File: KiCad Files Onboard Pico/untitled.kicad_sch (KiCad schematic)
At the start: 50 parts, among them J3 Button, J6 Conn_01x03_Male, U2 SOT-23-5 5.5V 3.3V 500mA, U4 RP2040, Y1 3225_4P 12MHz

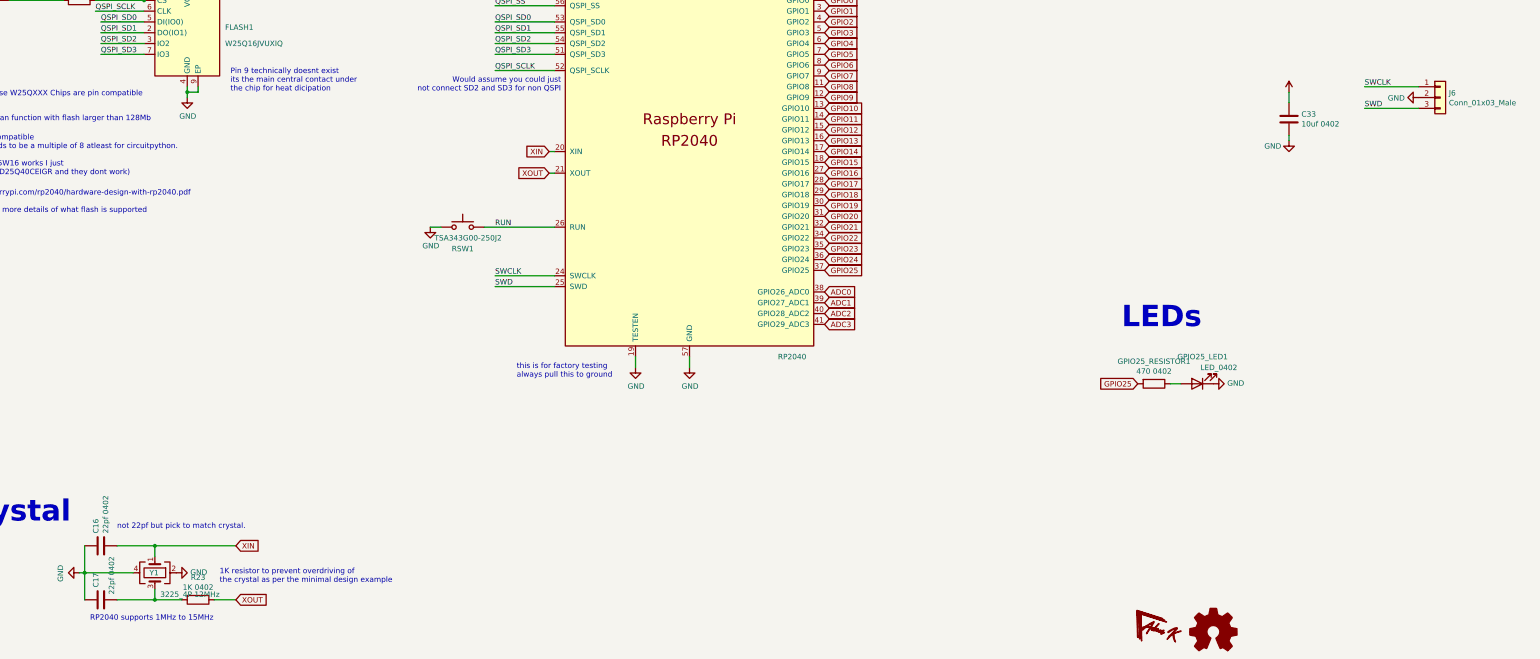
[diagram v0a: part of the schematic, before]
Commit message: Finished V1 Placement of onboard pico
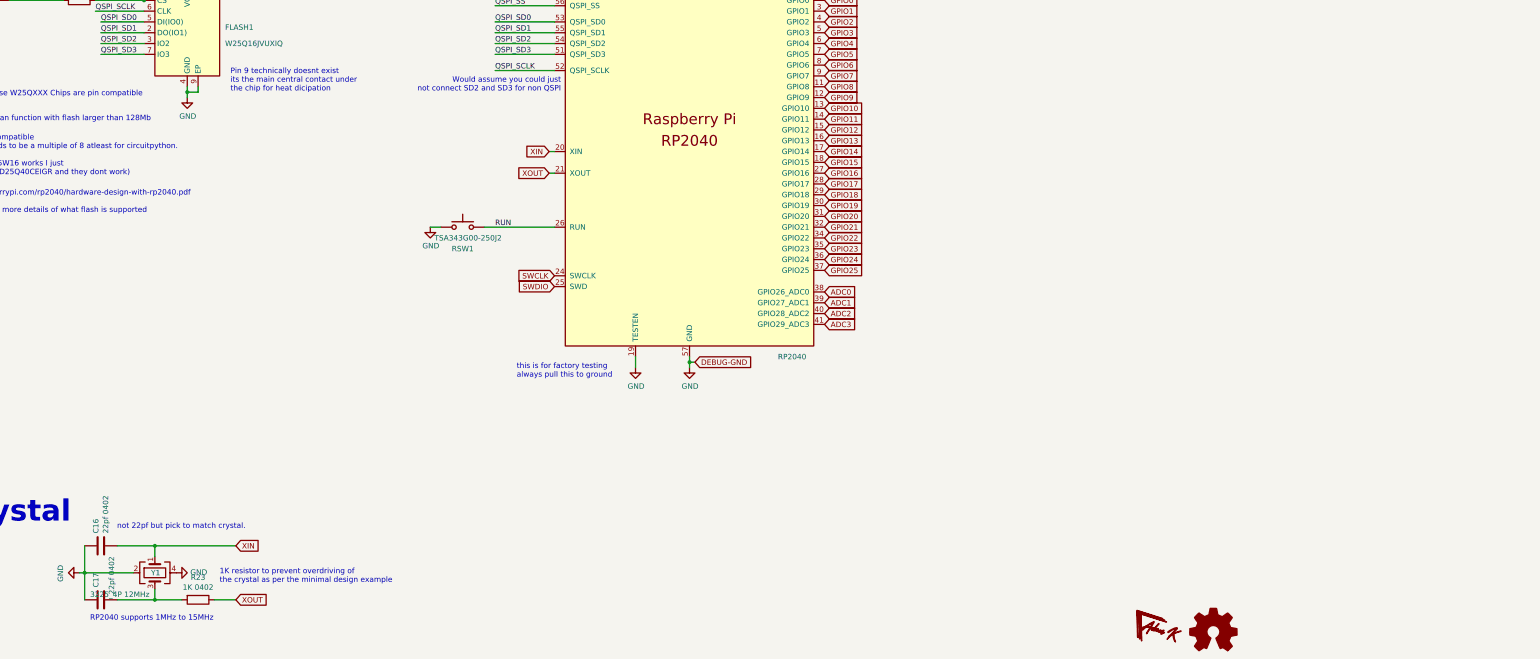
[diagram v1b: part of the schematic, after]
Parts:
- removed C33: 10uf 0402, Capacitor_SMD:C_0402_1005Metric, symbol Device:C
- removed GPIO25_LED1: LED_0402, LED_SMD:LED_0402_1005Metric, symbol Device:LED
- removed GPIO25_RESISTOR1: 470 0402, Resistor_SMD:R_0402_1005Metric, symbol Device:R
- removed J6: Conn_01x03_Male, Connector_PinHeader_2.54mm:PinHeader_1x03_P2.54mm_Vertical, symbol Connector_Generic:Conn_01x03
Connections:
- net SWD renamed SWDIO
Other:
- note removed: "LEDs"
- moved on the sheet: Y1

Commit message: fulkly wired v2
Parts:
- removed C32: 2.2uF 0402, Capacitor_SMD:C_0402_1005Metric, symbol Device:C
- removed R26: 200 0603, Resistor_SMD:R_0603_1608Metric, symbol Device:R_Small
- removed R27: 1 0402, Resistor_SMD:R_0402_1005Metric, symbol Device:R_Small
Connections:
- net +3V3: now also U4.43 (ADC_AVDD)
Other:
- note removed: "MAKE SURE THIS LINE is ran off of pin43 or close to pin43"
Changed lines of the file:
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@@
 (kicad_sch (version 20230121) (generator eeschema)
   (paper "A3")
-  (junction (at 292.1 90.17) (diameter 0) (color 0 0 0 0)
-  )
   (junction (at 139.7 44.45) (diameter 0) (color 0 0 0 0)
   )
@@
   (junction (at 212.09 81.28) (diameter 0) (color 0 0 0 0)
   )
+  (junction (at 215.9 81.28) (diameter 0) (color 0 0 0 0)
+  )
   (junction (at 273.05 60.96) (diameter 0) (color 0 0 0 0)
   )
@@
   )
   (junction (at 200.66 81.28) (diameter 0) (color 0 0 0 0)
-  )
-  (junction (at 292.1 78.74) (diameter 0) (color 0 0 0 0)
   )
   (junction (at 181.61 81.28) (diameter 0) (color 0 0 0 0)
@@
     (stroke (width 0) (type default))
   )
-  (wire (pts (xy 215.9 90.17) (xy 292.1 90.17))
-    (stroke (width 0) (type default))
-  )
   (wire (pts (xy 237.49 96.52) (xy 242.57 96.52))
     (stroke (width 0) (type default))
@@
     (stroke (width 0) (type default))
   )
-  (wire (pts (xy 292.1 78.74) (xy 292.1 81.28))
-    (stroke (width 0) (type default))
-  )
-  (wire (pts (xy 292.1 90.17) (xy 292.1 86.36))
-    (stroke (width 0) (type default))
-  )
   (wire (pts (xy 119.38 44.45) (xy 139.7 44.45))
     (stroke (width 0) (type default))
@@
     (stroke (width 0) (type default))
   )
-  (wire (pts (xy 215.9 93.98) (xy 215.9 90.17))
+  (wire (pts (xy 215.9 73.66) (xy 215.9 81.28))
     (stroke (width 0) (type default))
   )
@@
     (stroke (width 0) (type default))
   )
-  (wire (pts (xy 292.1 67.31) (xy 292.1 69.85))
-    (stroke (width 0) (type default))
-  )
   (wire (pts (xy 179.07 60.96) (xy 179.07 81.28))
     (stroke (width 0) (type default))
@@
     (stroke (width 0) (type default))
   )
+  (wire (pts (xy 215.9 81.28) (xy 215.9 93.98))
+    (stroke (width 0) (type default))
+  )
   (wire (pts (xy 15.24 87.63) (xy 26.67 87.63))
     (stroke (width 0) (type default))
@@
     (stroke (width 0) (type default))
   )
-  (wire (pts (xy 215.9 73.66) (xy 215.9 81.28))
-    (stroke (width 0) (type default))
-  )
   (wire (pts (xy 81.28 87.63) (xy 81.28 91.44))
     (stroke (width 0) (type default))
@@
     (stroke (width 0) (type default))
   )
-  (wire (pts (xy 292.1 74.93) (xy 292.1 78.74))
-    (stroke (width 0) (type default))
-  )
   (wire (pts (xy 87.63 96.52) (xy 87.63 97.79))
     (stroke (width 0) (type default))
@@
     (stroke (width 0) (type default))
   )
-  (wire (pts (xy 292.1 102.87) (xy 292.1 105.41))
-    (stroke (width 0) (type default))
-  )
   (wire (pts (xy 179.07 81.28) (xy 172.72 81.28))
     (stroke (width 0) (type default))
@@
   )
   (wire (pts (xy 215.9 60.96) (xy 215.9 73.66))
-    (stroke (width 0) (type default))
-  )
-  (wire (pts (xy 292.1 90.17) (xy 292.1 95.25))
-    (stroke (width 0) (type default))
-  )
-  (wire (pts (xy 292.1 78.74) (xy 306.07 78.74))
     (stroke (width 0) (type default))
   )
@@
   (text "RP2040 supports 1MHz to 15MHz" (at 58.42 257.81 0)
     (effects (font (size 1.27 1.27)) (justify left bottom))
-  )
-  (text "MAKE SURE THIS LINE \nis ran off of pin43\nor close to pin43"
-    (at 289.56 78.74 90)
-    (effects (font (size 0.5 0.5)) (justify left bottom))
   )
   (text "https://datasheets.raspberrypi.com/rp2040/hardware-design-with-rp2040.pdf\n\nOn page 13 you can learn more details of what flash is supported\n"
@@
   (label "QSPI_SD0" (at 153.67 116.84 0) (fields_autoplaced)
     (effects (font (size 1.27 1.27)) (justify left bottom))
-  )
-  (label "ADC_VREF" (at 306.07 78.74 180) (fields_autoplaced)
-    (effects (font (size 1.27 1.27)) (justify right bottom))
   )
   (label "QSPI_SD3" (at 153.67 124.46 0) (fields_autoplaced)
@@
         (path "/7b892ee5-f34f-4bca-8f87-a56522432f7c"
           (reference "#PWR06") (unit 1)
-        )
-      )
-    )
-  )
-  (symbol (lib_id "power:GND") (at 292.1 105.41 0) (unit 1)
-    (in_bom yes) (on_board yes) (dnp no)
-    (property "Reference" "#PWR079" (at 292.1 111.76 0)
-      (effects (font (size 1.27 1.27)) hide)
-    )
-    (property "Value" "GND" (at 292.227 109.8042 0)
-      (effects (font (size 1.27 1.27)))
-    )
-    (property "Footprint" "" (at 292.1 105.41 0)
-      (effects (font (size 1.27 1.27)) hide)
-    )
-    (property "Datasheet" "" (at 292.1 105.41 0)
-      (effects (font (size 1.27 1.27)) hide)
-    )
-    (pin "1")
-    (instances
-      (project "Env-MicroDotClock"
-        (path "/3dbeb8d8-208e-4f6d-8d30-b14372f68a4f/6b5c3b7c-d164-4e63-b354-b3df0a72db3d"
-          (reference "#PWR079") (unit 1)
-        )
-      )
-      (project "EnvOpenPico"
-        (path "/7b892ee5-f34f-4bca-8f87-a56522432f7c"
-          (reference "#PWR0101") (unit 1)
         )
       )
@@
     )
   )
-  (symbol (lib_id "Device:C") (at 292.1 99.06 0) (unit 1)
-    (in_bom yes) (on_board yes) (dnp no)
-    (property "Reference" "C32" (at 292.1 99.06 0)
-      (effects (font (size 0.5 0.5)))
-    )
-    (property "Value" "2.2uF 0402" (at 288.29 104.14 90)
-      (effects (font (size 1.27 1.27)) (justify left))
-    )
-    (property "Footprint" "Capacitor_SMD:C_0402_1005Metric" (at 293.0652 102.87 0)
-      (effects (font (size 1.27 1.27)) hide)
-    )
-    (property "Datasheet" "" (at 292.1 99.06 0)
-      (effects (font (size 1.27 1.27)) hide)
-    )
-    (property "LCSC" " " (at 292.1 99.06 0)
-      (effects (font (size 1.27 1.27)) hide)
-    )
-    (pin "1")
-    (pin "2")
-    (instances
-      (project "Env-MicroDotClock"
-        (path "/3dbeb8d8-208e-4f6d-8d30-b14372f68a4f/6b5c3b7c-d164-4e63-b354-b3df0a72db3d"
-          (reference "C32") (unit 1)
-        )
-      )
-      (project "EnvOpenPico"
-        (path "/7b892ee5-f34f-4bca-8f87-a56522432f7c"
-          (reference "C102") (unit 1)
-        )
-      )
-    )
-  )
   (symbol (lib_id "Regulator_Linear:AP131-15") (at 111.76 46.99 0) (unit 1)
     (in_bom yes) (on_board yes) (dnp no)
@@
     )
   )
-  (symbol (lib_id "power:+3.3V") (at 292.1 67.31 0) (unit 1)
-    (in_bom yes) (on_board yes) (dnp no)
-    (property "Reference" "#PWR078" (at 292.1 71.12 0)
-      (effects (font (size 1.27 1.27)) hide)
-    )
-    (property "Value" "+3.3V" (at 292.481 62.9158 0)
-      (effects (font (size 1.27 1.27)))
-    )
-    (property "Footprint" "" (at 292.1 67.31 0)
-      (effects (font (size 1.27 1.27)) hide)
-    )
-    (property "Datasheet" "" (at 292.1 67.31 0)
-      (effects (font (size 1.27 1.27)) hide)
-    )
-    (pin "1")
-    (instances
-      (project "Env-MicroDotClock"
-        (path "/3dbeb8d8-208e-4f6d-8d30-b14372f68a4f/6b5c3b7c-d164-4e63-b354-b3df0a72db3d"
-          (reference "#PWR078") (unit 1)
-        )
-      )
-      (project "EnvOpenPico"
-        (path "/7b892ee5-f34f-4bca-8f87-a56522432f7c"
-          (reference "#PWR013") (unit 1)
-        )
-      )
-    )
-  )
   (symbol (lib_id "power:GND") (at 81.28 134.62 0) (unit 1)
     (in_bom yes) (on_board yes) (dnp no)
@@
     )
   )
-  (symbol (lib_id "Device:R_Small") (at 292.1 83.82 0) (unit 1)
-    (in_bom yes) (on_board yes) (dnp no)
-    (property "Reference" "R27" (at 293.5986 82.6516 0)
-      (effects (font (size 1.27 1.27)) (justify left))
-    )
-    (property "Value" "1 0402" (at 293.5986 84.963 0)
-      (effects (font (size 1.27 1.27)) (justify left))
-    )
-    (property "Footprint" "Resistor_SMD:R_0402_1005Metric" (at 292.1 83.82 0)
-      (effects (font (size 1.27 1.27)) hide)
-    )
-    (property "Datasheet" "" (at 292.1 83.82 0)
-      (effects (font (size 1.27 1.27)) hide)
-    )
-    (property "LCSC" " " (at 292.1 83.82 0)
-      (effects (font (size 1.27 1.27)) hide)
-    )
-    (pin "1")
-    (pin "2")
-    (instances
-      (project "Env-MicroDotClock"
-        (path "/3dbeb8d8-208e-4f6d-8d30-b14372f68a4f/6b5c3b7c-d164-4e63-b354-b3df0a72db3d"
-          (reference "R27") (unit 1)
-        )
-      )
-      (project "EnvOpenPico"
-        (path "/7b892ee5-f34f-4bca-8f87-a56522432f7c"
-          (reference "R10") (unit 1)
-        )
-      )
-    )
-  )
   (symbol (lib_id "Device:FerriteBead_Small") (at 91.44 44.45 90) (unit 1)
     (in_bom yes) (on_board yes) (dnp no) (fields_autoplaced)
@@
         )
       )
-    )
-  )
-  (symbol (lib_id "Device:R_Small") (at 292.1 72.39 0) (unit 1)
-    (in_bom yes) (on_board yes) (dnp no)
-    (property "Reference" "R26" (at 293.5986 71.2216 0)
-      (effects (font (size 1.27 1.27)) (justify left))
-    )
-    (property "Value" "200 0603" (at 293.5986 73.533 0)
-      (effects (font (size 1.27 1.27)) (justify left))
-    )
-    (property "Footprint" "Resistor_SMD:R_0603_1608Metric" (at 292.1 72.39 0)
-      (effects (font (size 1.27 1.27)) hide)
-    )
-    (property "Datasheet" "" (at 292.1 72.39 0)
-      (effects (font (size 1.27 1.27)) hide)
-    )
-    (property "LCSC" " " (at 292.1 72.39 0)
-      (effects (font (size 1.27 1.27)) hide)
-    )
-    (pin "1")
-    (pin "2")
-    (instances
-      (project "Env-MicroDotClock"
-        (path "/3dbeb8d8-208e-4f6d-8d30-b14372f68a4f/6b5c3b7c-d164-4e63-b354-b3df0a72db3d"
-          (reference "R26") (unit 1)
-        )
-      )
-      (project "EnvOpenPico"
-        (path "/7b892ee5-f34f-4bca-8f87-a56522432f7c"
-          (reference "R9") (unit 1)
-        )
-      )

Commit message: began rework of onboard 2040 pcb
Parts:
- removed C15: 0.1uf 0402, Capacitor_SMD:C_0402_1005Metric, symbol Device:C
- removed NT1: NetTie_2, NetTie:NetTie-2_SMD_Pad0.5mm, symbol Device:NetTie_2
- removed R17: 220 0402, Resistor_SMD:R_0402_1005Metric, symbol Device:R
- removed R19: 5.6K 0402, Resistor_SMD:R_0402_1005Metric, symbol Device:R
- removed R20: 10K 0402, Resistor_SMD:R_0402_1005Metric, symbol Device:R
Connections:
- net GND: now also USB1.13 (SHIELD)
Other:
- note removed: "I think this is important for usb 3.0 but not 2.0 and 1.1 however it may help with analogue performance but ive yet to test this"
- note removed: "VBUS SENSE"

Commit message: finished up and cleaned up PCB, added logos
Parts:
- U2: value SOT-23-5 5.5V 3.3V 500mA -> TLV75733PDBVR
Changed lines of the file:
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@@
       (effects (font (size 1.27 1.27)))
     )
-    (property "Value" "SOT-23-5 5.5V 3.3V 500mA" (at 111.76 40.6146 0)
+    (property "Value" "TLV75733PDBVR" (at 111.76 40.6146 0)
       (effects (font (size 1.27 1.27)))
     )

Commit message: added thermal vias, improved gnd connections from IS31FL37s, added thermal vias, added power only usb port on the back.
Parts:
- removed USB1: TYPE-C-31-M-12, Connector_USB:USB_C_Receptacle_HRO_TYPE-C-31-M-12, symbol Type-C:HRO-TYPE-C-31-M-12
- added D2: 1N4002W, Diode_SMD:D_SOD-123, symbol Device:D_Schottky
- added J2: GT-USB-7051A, Connector_USB:USB_C_Receptacle_G-Switch_GT-USB-7051x, symbol Connector:USB_C_Receptacle_USB2.0_16P
- added J4: TYPE-C-31-M-12, Connector_USB:USB_C_Receptacle_HRO_TYPE-C-31-M-12, symbol Connector:USB_C_Receptacle_USB2.0_16P
- added R14, R17: 5.1K 0805, Resistor_SMD:R_0805_2012Metric, symbol Device:R_Small
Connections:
- net GND: now also J2.A1 (GND), J2.A12 (GND), J2.B1 (GND), J2.B12 (GND), J2.S1 (SHIELD), J4.A1 (GND), J4.A12 (GND), J4.B1 (GND), J4.B12 (GND), J4.S1 (SHIELD), R14.1, R17.1
- net USB_D+: now also J4.A6 (D+), J4.B6 (D+)
- net USB_D-: now also J4.A7 (D-), J4.B7 (D-)
- net VBUS: now also J4.A4 (VBUS), J4.A9 (VBUS), J4.B4 (VBUS), J4.B9 (VBUS)
- net VSYS: now also D2.1 (K)
- net at R16.2: now also J4.A5 (CC1)
- net at R15.2: now also J4.B5 (CC2)
- new net: J2.A5 (CC1), R14.2
- new net: D2.2 (A), J2.A4 (VBUS), J2.A9 (VBUS), J2.B4 (VBUS), J2.B9 (VBUS)
- new net: J2.B5 (CC2), R17.2
- no-connect marks 2 -> 0
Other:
- moved on the sheet: D1, R15, R16

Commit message: swapped LDO for more capable switching regulator.
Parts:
- removed C19, C20, CBP1: 10uf 0402, Capacitor_SMD:C_0402_1005Metric, symbol Device:C
- removed F1: 0805L050WR, Fuse:Fuse_0805_2012Metric, symbol Device:Polyfuse_Small
- removed FB1: FerriteBead 0402, Resistor_SMD:R_0402_1005Metric, symbol Device:FerriteBead_Small
- removed R22: 100K 0402, Resistor_SMD:R_0402_1005Metric, symbol Device:R
- removed U2: TLV75733PDBVR, Package_TO_SOT_SMD:SOT-23-5, symbol Regulator_Linear:AP131-15
- added C15, C20, C32: 10uF 0402, Capacitor_SMD:C_0402_1005Metric, symbol Device:C_Small
- added C19: 0.1uF 0402, Capacitor_SMD:C_0402_1005Metric, symbol Device:C_Small
- added L1: SPH3015H2R2MT, Inductor_SMD:L_Sunlord_SWPA3015S, symbol Device:L_Small
- added R19: 100ohm 0402, Resistor_SMD:R_0402_1005Metric, symbol Device:R_Small
- added U2: TPS63001DRCR, Package_SON:Texas_DRC0010J_ThermalVias, symbol Regulator_Switching:TPS63001
- D1, D2: value 1N4002W -> 1N5819W
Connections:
- net +3V3: now also C20.1, C32.1, U2.1 (VOUT), U2.10 (FB)
- net GND: now also C15.2, C19.2, C20.2, C32.2, U2.11 (PGND), U2.3 (PGND), U2.9 (GND)
- net VSYS: now also C15.1, R19.1, U2.5 (VIN)
- net VBUS: no longer names the net of D1.2 (A), J4.A4 (VBUS), J4.A9 (VBUS), J4.B4 (VBUS), J4.B9 (VBUS)
- new net: L1.1, U2.4 (L1)
- new net: L1.2, U2.2 (L2)
- new net: C19.1, R19.2, U2.6 (EN), U2.7 (PS/SYNC), U2.8 (VINA)
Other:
- note removed: "500mA hold current 1A trip 6V trip"
- note removed: "D1 NEEDS to be 0omh resistor or 1N4002 diode"
- note removed: "GPIOs"
- note removed: "Only fit cBP1 if you have selected an alternate voltage regulator TLV75533PDBVR does not require cBP1."
- note removed: "USB/POWER"

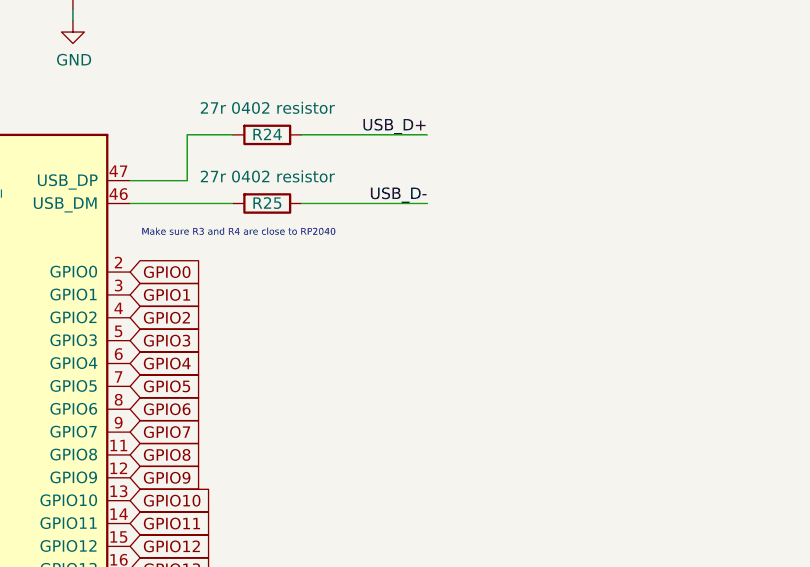
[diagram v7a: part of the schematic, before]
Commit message: Moved all ICs to one i2c bus, removed SI7021, added i2c level shifters.
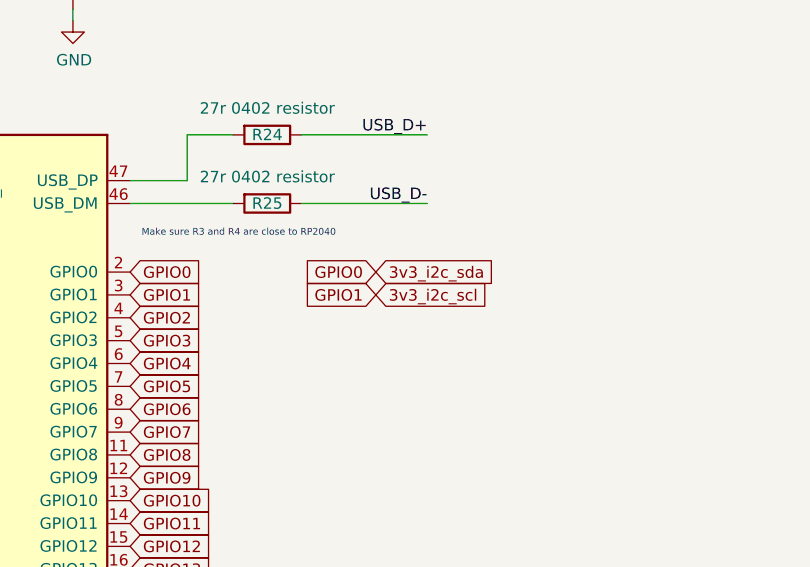
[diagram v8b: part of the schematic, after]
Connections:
- net GPIO0 renamed 3v3_i2c_sda
- net GPIO1 renamed 3v3_i2c_scl
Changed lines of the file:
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@@
+		)
+	)
+	(global_label "GPIO0"
+		(shape input)
+		(at 258.445 111.76 180)
+		(fields_autoplaced yes)
+		(effects
+			(font
+				(size 1.27 1.27)
+			)
+			(justify right)
+		)
+		(property "Intersheetrefs" "${INTERSHEET_REFS}"
+			(at 249.775 111.76 0)
+			(effects
+				(font
+					(size 1.27 1.27)
+				)
+				(justify right)
+				(hide yes)
+			)
+		)
+	)
+	(global_label "3v3_i2c_sda"
+		(shape input)
+		(at 258.445 111.76 0)
+		(fields_autoplaced yes)
+		(effects
+			(font
+				(size 1.27 1.27)
+			)
+			(justify left)
+		)
+		(property "Intersheetrefs" "${INTERSHEET_REFS}"
+			(at 272.981 111.76 0)
+			(effects
+				(font
+					(size 1.27 1.27)
+				)
+				(justify left)
+				(hide yes)
+			)
 		)
 	)
@@
 		)
 	)
+	(global_label "3v3_i2c_scl"
+		(shape input)
+		(at 258.445 114.3 0)
+		(fields_autoplaced yes)
+		(effects
+			(font
+				(size 1.27 1.27)
+			)
+			(justify left)
+		)
+		(property "Intersheetrefs" "${INTERSHEET_REFS}"
+			(at 272.4368 114.3 0)
+			(effects
+				(font
+					(size 1.27 1.27)
+				)
+				(justify left)
+				(hide yes)
+			)
+		)
+	)
 	(global_label "USB_D+"
 		(shape input)
@@
 				(hide yes)
 			)
+		)
+	)
+	(global_label "GPIO1"
+		(shape input)
+		(at 258.445 114.3 180)
+		(fields_autoplaced yes)
+		(effects
+			(font
+				(size 1.27 1.27)
+			)
+			(justify right)
+		)
+		(property "Intersheetrefs" "${INTERSHEET_REFS}"
+			(at 249.775 114.3 0)
+			(effects
+				(font
+					(size 1.27 1.27)
+				)
+				(justify right)
+				(hide yes)
+			)
